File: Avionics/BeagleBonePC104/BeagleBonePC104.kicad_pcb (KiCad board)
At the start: 2 copper layers, 90.2 x 95.9 mm, 17 parts, among them U5 TMP36xS

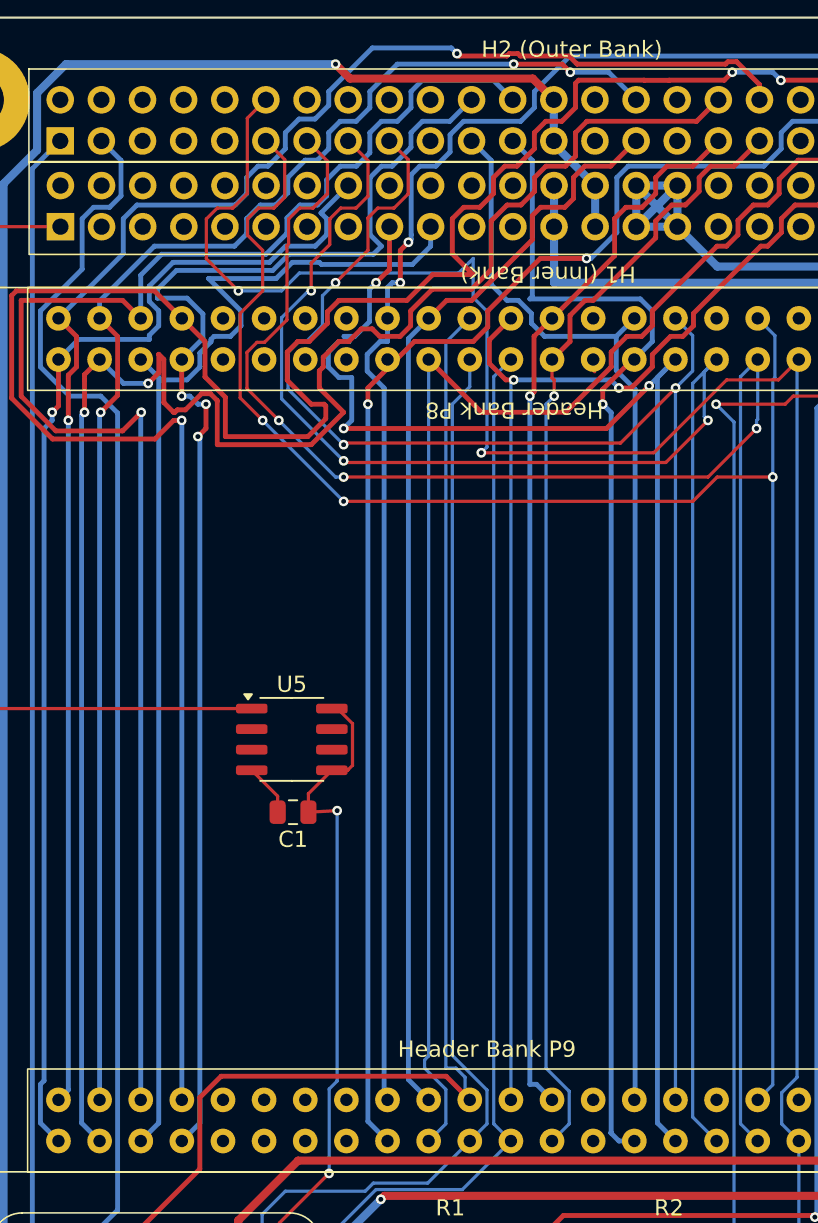
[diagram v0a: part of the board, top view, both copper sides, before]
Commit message: Ian Goldberg - Corrected DRC errors on battery board and generated gerber files to order
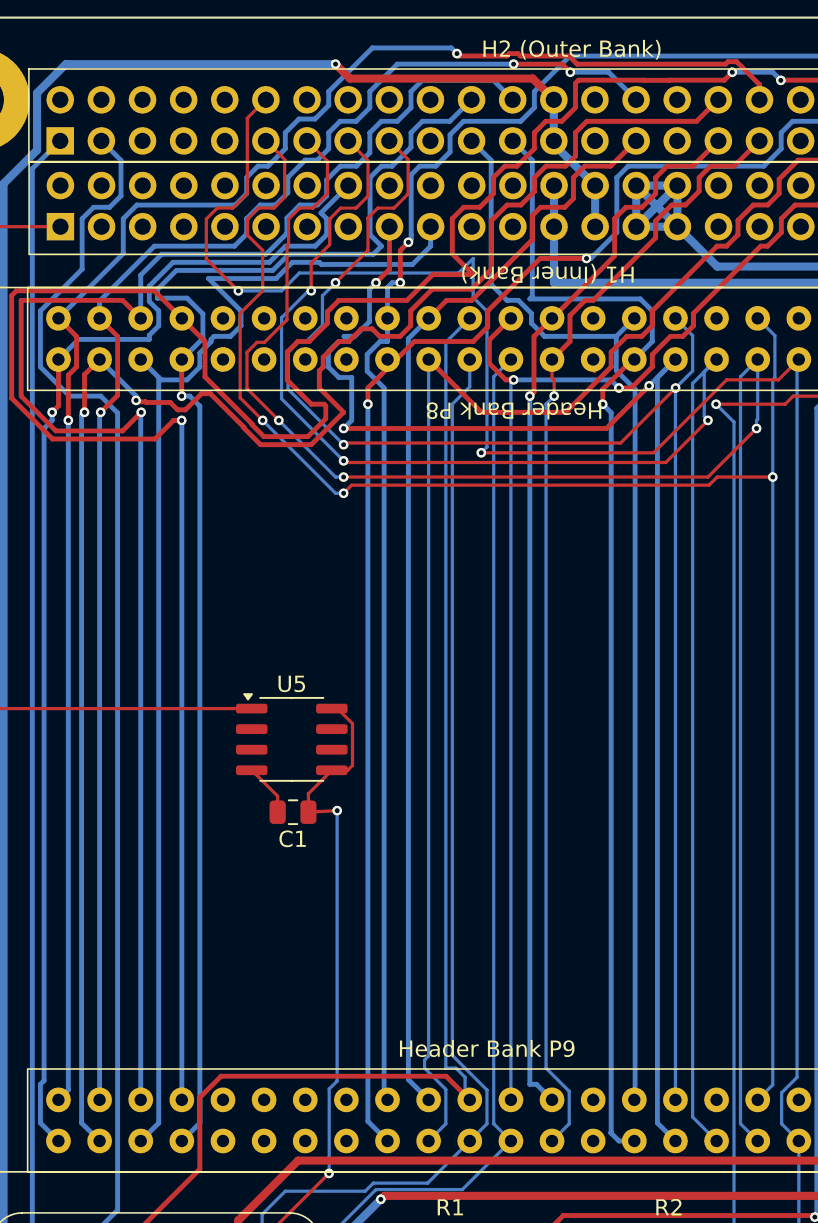
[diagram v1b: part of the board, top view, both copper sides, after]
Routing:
- net /GPIO2_9: track 112.7 -> 107.5 mm
- net /GPIO2_12: track 145.8 -> 144.4 mm
- net /GPIO2_13: track 85.6 -> 84.8 mm, vias 3 -> 1
